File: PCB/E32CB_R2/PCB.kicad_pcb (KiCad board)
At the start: 2 copper layers, 121.4 x 90.9 mm, 88 parts, among them J1 GND, J10 VM1, J11 GND, J12 VM2, J13 GND, J14 P3B, J15 GND, J16 P3A, J17 NEXTION, J18 Power, J19 OneWire, J2 pump, J20 I2C, J3 GND, J4 LED, J5 GND, J6 P12B, J7 GND, J8 P12A, J9 GND, Q1 S8050, Q10 IRLR2905, Q2 S8050, Q3 IRLR2905, Q4 IRLR2905, Q5 IRLR2905, Q6 IRLR2905, Q7 IRLR2905, Q8 IRLR2905, Q9 IRLR2905, X1 12MHz

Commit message: pcb update
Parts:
- removed C9: 2.2uF, Capacitor_SMD:CP_Elec_4x5.4
- added REF**: C_0805_HandSoldering, Capacitors_SMD:C_0805_HandSoldering, B.Cu at (134.4, 71.9)
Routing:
- net +3V3: track 243.4 -> 245.6 mm
- net GND: vias 57 -> 54
- removed copper zone on B.Cu, net GND
- removed copper zone on F.Cu, net GND
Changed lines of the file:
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@@
     (thickness 1.6)
     (drawings 30)
-    (tracks 850)
+    (tracks 847)
     (zones 0)
     (modules 88)
@@
     (34 B.Paste user hide)
     (35 F.Paste user)
-    (36 B.SilkS user)
+    (36 B.SilkS user hide)
     (37 F.SilkS user)
-    (38 B.Mask user)
-    (39 F.Mask user hide)
-    (40 Dwgs.User user hide)
+    (38 B.Mask user hide)
+    (39 F.Mask user)
+    (40 Dwgs.User user)
     (41 Cmts.User user hide)
     (42 Eco1.User user)
@@
   )
   (setup
-    (last_trace_width 0.5)
+    (last_trace_width 0.75)
     (user_trace_width 0.2)
     (user_trace_width 0.254)
@@
     (mod_text_size 1 1)
     (mod_text_width 0.15)
-    (pad_size 1.524 1.524)
-    (pad_drill 0.762)
+    (pad_size 1.5 1.25)
+    (pad_drill 0)
     (pad_to_mask_clearance 0.051)
     (solder_mask_min_width 0.25)
@@
     (add_net "Net-(fan_3-Pad3)")
   )
+  (module Capacitors_SMD:C_0805_HandSoldering (layer B.Cu)
+    (at 134.366 71.882 180)
+    (descr "Capacitor SMD 0805, hand soldering")
+    (tags "capacitor 0805")
+    (attr smd)
+    (fp_text reference REF** (at 0 1.75) (layer B.SilkS)
+      (effects (font (size 1 1) (thickness 0.15)) (justify mirror))
+    )
+    (fp_text value C_0805_HandSoldering (at 0 -1.75) (layer B.Fab)
+      (effects (font (size 1 1) (thickness 0.15)) (justify mirror))
+    )
+    (fp_line (start 2.25 -0.87) (end -2.25 -0.87) (layer B.CrtYd) (width 0.05))
+    (fp_line (start 2.25 -0.87) (end 2.25 0.88) (layer B.CrtYd) (width 0.05))
+    (fp_line (start -2.25 0.88) (end -2.25 -0.87) (layer B.CrtYd) (width 0.05))
+    (fp_line (start -2.25 0.88) (end 2.25 0.88) (layer B.CrtYd) (width 0.05))
+    (fp_line (start -0.5 -0.85) (end 0.5 -0.85) (layer B.SilkS) (width 0.12))
+    (fp_line (start 0.5 0.85) (end -0.5 0.85) (layer B.SilkS) (width 0.12))
+    (fp_line (start -1 0.62) (end 1 0.62) (layer B.Fab) (width 0.1))
+    (fp_line (start 1 0.62) (end 1 -0.62) (layer B.Fab) (width 0.1))
+    (fp_line (start 1 -0.62) (end -1 -0.62) (layer B.Fab) (width 0.1))
+    (fp_line (start -1 -0.62) (end -1 0.62) (layer B.Fab) (width 0.1))
+    (fp_text user %R (at 0 1.75) (layer B.Fab)
+      (effects (font (size 1 1) (thickness 0.15)) (justify mirror))
+    )
+    (pad 2 smd rect (at 1.25 0 180) (size 1.5 1.25) (layers B.Cu B.Paste B.Mask)
+      (net 56 /s_LED))
+    (pad 1 smd rect (at -1.25 0 180) (size 1.5 1.25) (layers B.Cu B.Paste B.Mask)
+      (net 2 +3V3))
+    (model Capacitors_SMD.3dshapes/C_0805.wrl
+      (at (xyz 0 0 0))
+      (scale (xyz 1 1 1))
+      (rotate (xyz 0 0 0))
+    )
+  )
   (module Symbol:WEEE-Logo_5.6x8mm_SilkScreen (layer B.Cu)
     (at 157.48 79.375 180)
@@
     )
   )
-  (module Capacitor_SMD:CP_Elec_4x5.4 (layer F.Cu)
-    (at 147.32 62.23 270)
-    (descr "SMD capacitor, aluminum electrolytic, Panasonic A5 / Nichicon, 4.0x5.4mm")
-    (tags "capacitor electrolytic")
-    (attr smd)
-    (fp_text reference C9 (at 0 -3.2 90) (layer F.SilkS)
-      (effects (font (size 1 1) (thickness 0.15)))
-    )
-    (fp_text value 2.2uF (at 0 3.2 90) (layer F.Fab)
-      (effects (font (size 1 1) (thickness 0.15)))
-    )
-    (fp_text user %R (at 0 0 90) (layer F.Fab)
-      (effects (font (size 0.8 0.8) (thickness 0.12)))
-    )
-    (fp_line (start -3.35 1.05) (end -2.4 1.05) (layer F.CrtYd) (width 0.05))
-    (fp_line (start -3.35 -1.05) (end -3.35 1.05) (layer F.CrtYd) (width 0.05))
-    (fp_line (start -2.4 -1.05) (end -3.35 -1.05) (layer F.CrtYd) (width 0.05))
-    (fp_line (start -2.4 1.05) (end -2.4 1.25) (layer F.CrtYd) (width 0.05))
-    (fp_line (start -2.4 -1.25) (end -2.4 -1.05) (layer F.CrtYd) (width 0.05))
-    (fp_line (start -2.4 -1.25) (end -1.25 -2.4) (layer F.CrtYd) (width 0.05))
-    (fp_line (start -2.4 1.25) (end -1.25 2.4) (layer F.CrtYd) (width 0.05))
-    (fp_line (start -1.25 -2.4) (end 2.4 -2.4) (layer F.CrtYd) (width 0.05))
-    (fp_line (start -1.25 2.4) (end 2.4 2.4) (layer F.CrtYd) (width 0.05))
-    (fp_line (start 2.4 1.05) (end 2.4 2.4) (layer F.CrtYd) (width 0.05))
-    (fp_line (start 3.35 1.05) (end 2.4 1.05) (layer F.CrtYd) (width 0.05))
-    (fp_line (start 3.35 -1.05) (end 3.35 1.05) (layer F.CrtYd) (width 0.05))
-    (fp_line (start 2.4 -1.05) (end 3.35 -1.05) (layer F.CrtYd) (width 0.05))
-    (fp_line (start 2.4 -2.4) (end 2.4 -1.05) (layer F.CrtYd) (width 0.05))
-    (fp_line (start -2.75 -1.81) (end -2.75 -1.31) (layer F.SilkS) (width 0.12))
-    (fp_line (start -3 -1.56) (end -2.5 -1.56) (layer F.SilkS) (width 0.12))
-    (fp_line (start -2.26 1.195563) (end -1.195563 2.26) (layer F.SilkS) (width 0.12))
-    (fp_line (start -2.26 -1.195563) (end -1.195563 -2.26) (layer F.SilkS) (width 0.12))
-    (fp_line (start -2.26 -1.195563) (end -2.26 -1.06) (layer F.SilkS) (width 0.12))
-    (fp_line (start -2.26 1.195563) (end -2.26 1.06) (layer F.SilkS) (width 0.12))
-    (fp_line (start -1.195563 2.26) (end 2.26 2.26) (layer F.SilkS) (width 0.12))
-    (fp_line (start -1.195563 -2.26) (end 2.26 -2.26) (layer F.SilkS) (width 0.12))
-    (fp_line (start 2.26 -2.26) (end 2.26 -1.06) (layer F.SilkS) (width 0.12))
-    (fp_line (start 2.26 2.26) (end 2.26 1.06) (layer F.SilkS) (width 0.12))
-    (fp_line (start -1.374773 -1.2) (end -1.374773 -0.8) (layer F.Fab) (width 0.1))
-    (fp_line (start -1.574773 -1) (end -1.174773 -1) (layer F.Fab) (width 0.1))
-    (fp_line (start -2.15 1.15) (end -1.15 2.15) (layer F.Fab) (width 0.1))
-    (fp_line (start -2.15 -1.15) (end -1.15 -2.15) (layer F.Fab) (width 0.1))
-    (fp_line (start -2.15 -1.15) (end -2.15 1.15) (layer F.Fab) (width 0.1))
-    (fp_line (start -1.15 2.15) (end 2.15 2.15) (layer F.Fab) (width 0.1))
-    (fp_line (start -1.15 -2.15) (end 2.15 -2.15) (layer F.Fab) (width 0.1))
-    (fp_line (start 2.15 -2.15) (end 2.15 2.15) (layer F.Fab) (width 0.1))
-    (fp_circle (center 0 0) (end 2 0) (layer F.Fab) (width 0.1))
-    (pad 2 smd roundrect (at 1.8 0 270) (size 2.6 1.6) (layers F.Cu F.Paste F.Mask) (roundrect_rratio 0.15625)
-      (net 1 GND))
-    (pad 1 smd roundrect (at -1.8 0 270) (size 2.6 1.6) (layers F.Cu F.Paste F.Mask) (roundrect_rratio 0.15625)
-      (net 2 +3V3))
-    (model ${KISYS3DMOD}/Capacitor_SMD.3dshapes/CP_Elec_4x5.4.wrl
-      (at (xyz 0 0 0))
-      (scale (xyz 1 1 1))
-      (rotate (xyz 0 0 0))
-    )
-  )
   (module Capacitors_SMD:C_1206_HandSoldering (layer B.Cu)
     (at 158.496 66.834 270)
@@
   (via (at 124.46 73.66) (size 0.8) (drill 0.4) (layers F.Cu B.Cu) (net 1))
   (via (at 119.38 69.85) (size 0.8) (drill 0.4) (layers F.Cu B.Cu) (net 1))
-  (via (at 167.64 67.31) (size 0.8) (drill 0.4) (layers F.Cu B.Cu) (net 1))
-  (via (at 165.1 67.31) (size 0.8) (drill 0.4) (layers F.Cu B.Cu) (net 1))
-  (via (at 166.37 66.04) (size 0.8) (drill 0.4) (layers F.Cu B.Cu) (net 1))
   (via (at 102.87 59.69) (size 0.8) (drill 0.4) (layers F.Cu B.Cu) (net 1))
   (via (at 101.6 55.88) (size 0.8) (drill 0.4) (layers F.Cu B.Cu) (net 1))
@@
   (via (at 139.245 70.305) (size 0.8) (drill 0.4) (layers F.Cu B.Cu) (net 2))
   (segment (start 138.43 71.12) (end 139.245 70.305) (width 0.75) (layer F.Cu) (net 2))
-  (segment (start 139.245 68.505) (end 147.32 60.43) (width 0.75) (layer F.Cu) (net 2))
-  (segment (start 199.39 60.96) (end 198.12 59.69) (width 0.75) (layer F.Cu) (net 2))
-  (segment (start 199.39 66.04) (end 199.39 60.96) (width 0.75) (layer F.Cu) (net 2))
-  (segment (start 198.12 59.69) (end 149.86 59.69) (width 0.75) (layer F.Cu) (net 2))
-  (segment (start 149.12 60.43) (end 147.32 60.43) (width 0.75) (layer F.Cu) (net 2))
-  (segment (start 149.86 59.69) (end 149.12 60.43) (width 0.75) (layer F.Cu) (net 2))
   (segment (start 124.46 68.58) (end 139.192 68.58) (width 0.75) (layer F.Cu) (net 2))
-  (segment (start 139.192 68.58) (end 139.245 68.505) (width 0.75) (layer F.Cu) (net 2))
   (segment (start 139.245 70.305) (end 139.192 68.58) (width 0.75) (layer F.Cu) (net 2))
   (segment (start 139.245 68.575) (end 139.245 70.305) (width 1.5) (layer B.Cu) (net 2))
@@
   (segment (start 176.53 67.47) (end 176.53 67.056) (width 0.5) (layer B.Cu) (net 2))
   (segment (start 176.53 67.056) (end 176.53 62.23) (width 0.5) (layer B.Cu) (net 2))
+  (segment (start 139.245 68.505) (end 139.192 68.58) (width 0.75) (layer F.Cu) (net 2))
+  (segment (start 147.806 59.944) (end 139.245 68.505) (width 0.75) (layer F.Cu) (net 2))
+  (segment (start 197.177516 59.944) (end 147.806 59.944) (width 0.75) (layer F.Cu) (net 2))
+  (segment (start 199.39 66.04) (end 199.39 62.156484) (width 0.75) (layer F.Cu) (net 2))
+  (segment (start 199.39 62.156484) (end 197.177516 59.944) (width 0.75) (layer F.Cu) (net 2))
+  (segment (start 137.668 71.882) (end 138.43 71.12) (width 0.75) (layer B.Cu) (net 2))
+  (segment (start 135.616 71.882) (end 137.668 71.882) (width 0.75) (layer B.Cu) (net 2))
   (segment (start 193.04 50.825) (end 190.475 48.26) (width 1.5) (layer B.Cu) (net 3))
   (segment (start 193.04 53.34) (end 193.04 50.825) (width 1.5) (layer B.Cu) (net 3))
@@
   (segment (start 185.928 93.98) (end 189.23 90.678) (width 0.254) (layer B.Cu) (net 65))
   (segment (start 158.75 94.488) (end 159.258 93.98) (width 0.254) (layer B.Cu) (net 65))
-  (zone (net 1) (net_name GND) (layer F.Cu) (hatch edge 0.508)
-    (connect_pads (clearance 0.508))
-    (min_thickness 0.254)
-    (fill yes (arc_segments 32) (thermal_gap 0.508) (thermal_bridge_width 0.508))
-    (polygon
-      (pts
-        (xy 208.026 136.906) (xy 86.614 136.906) (xy 86.614 45.974) (xy 208.026 45.974)
-      )
-    )
-  )
-  (zone (net 1) (net_name GND) (layer B.Cu) (hatch edge 0.508)
-    (connect_pads (clearance 0.508))
-    (min_thickness 0.254)
-    (fill yes (arc_segments 32) (thermal_gap 0.508) (thermal_bridge_width 0.508))
-    (polygon
-      (pts
-        (xy 208.026 136.906) (xy 86.614 136.906) (xy 86.614 45.974) (xy 208.026 45.974)
-      )
-    )
-  )
 )

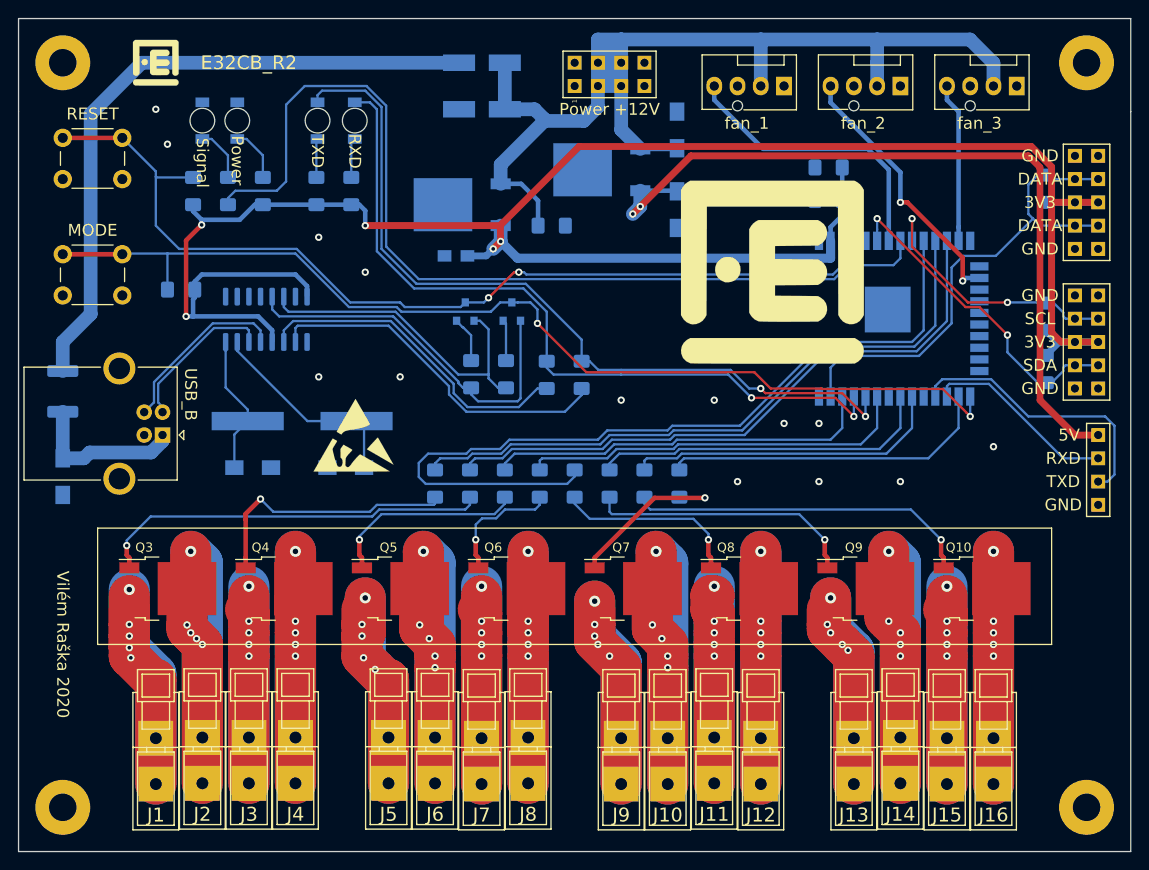
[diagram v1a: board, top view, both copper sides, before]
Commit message: 1206 to 0805
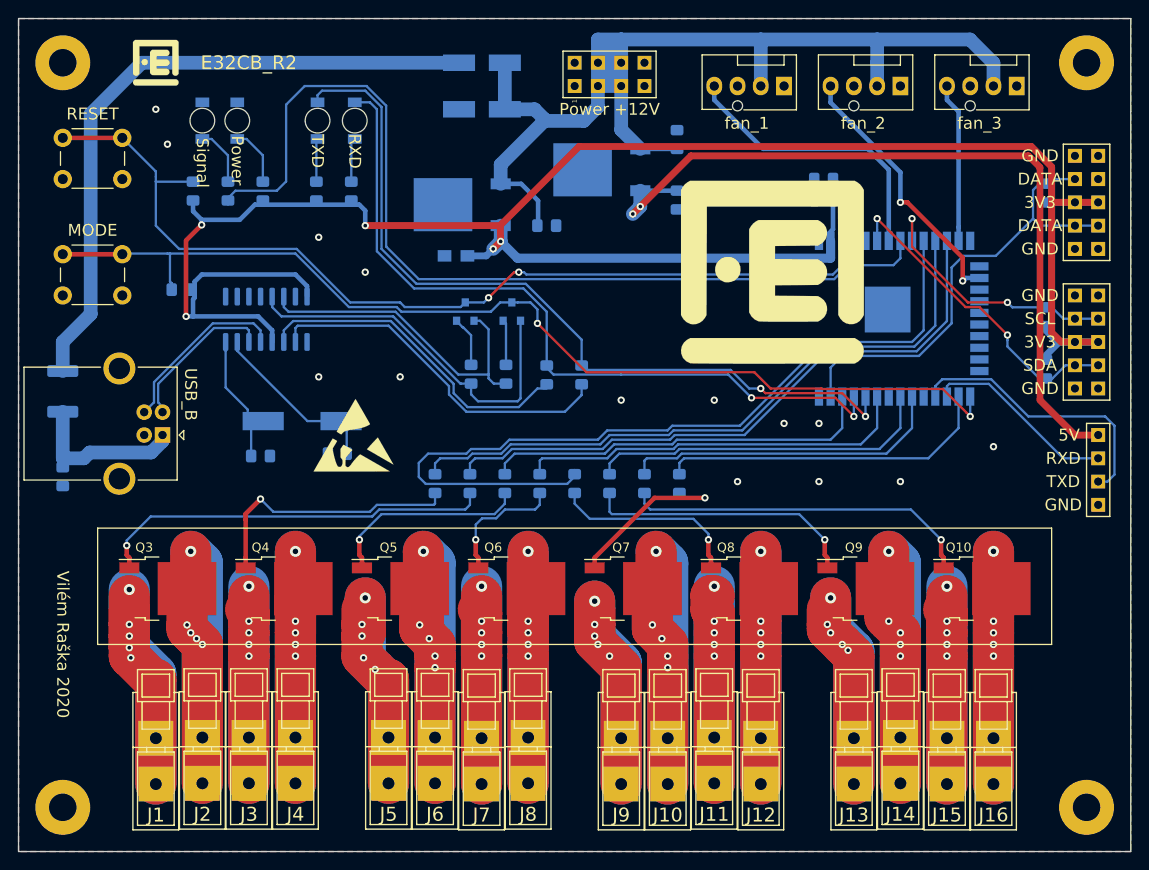
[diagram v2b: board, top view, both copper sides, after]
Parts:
- C1, C2, C3, C6, C8: footprint Capacitors_SMD:C_1206_HandSoldering -> Capacitor_SMD:C_0805_2012Metric_Pad1.15x1.40mm_HandSolder
- C4, C5, C7: footprint Capacitor_SMD:C_1206_3216Metric_Pad1.42x1.75mm_HandSolder -> Capacitor_SMD:C_0805_2012Metric_Pad1.15x1.40mm_HandSolder
- R1, R10, R11, R12, R13, R14, R15, R16, R17, R18, R19, R2, R20, R21, R3, R4, R5, R6, R7, R8, R9: footprint Resistor_SMD:R_1206_3216Metric_Pad1.42x1.75mm_HandSolder -> Resistor_SMD:R_0805_2012Metric_Pad1.15x1.40mm_HandSolder
- X1: footprint Crystals:Crystal_SMD_HC49-SD_HandSoldering -> Crystals:Crystal_SMD_HC49-SD
- moved C1 1.78 mm to (121.4, 93.5)
- moved C2 1.53 mm to (113.0, 93.7)
- moved C5 1.38 mm to (174.5, 63.5)
- moved C6 1.05 mm to (158.5, 59.2)
- moved C8 1.05 mm to (158.5, 65.8)
- moved C4 0.54 mm to (174.5, 65.8)
- moved C7 0.54 mm to (144.3, 68.6)
- moved R1 0.47 mm to (198.8, 65.0)
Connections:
- REF** pad 2: /s_LED -> GND
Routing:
- net /OneWire: track 55.2 -> 51.2 mm
- net Net-(C2-Pad1): track 15.3 -> 13.6 mm
- net +3V3: track 245.6 -> 244.0 mm
- net Net-(C1-Pad1): track 22.6 -> 21.2 mm
- net /I2C_SDA: track 36.2 -> 35.1 mm
- added copper zone on B.Cu, net (none)
- added copper zone on F.Cu, net GND
